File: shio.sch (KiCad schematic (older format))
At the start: 36 parts

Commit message: Few additions
- Added USB micro
- Added 2 LEDs
- Swapped NOR for NAND memory
- Added test points
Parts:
- removed U?: W25Q16JVSSIQ, SOIC127P790X216-8N, symbol W25Q16JVSSIQ:W25Q16JVSSIQ
- added AE?: Antenna_Chip, symbol Device:Antenna_Chip
- added D?: LED1, symbol Device:LED_Small_ALT
- added D?: LED2, symbol Device:LED_Small_ALT
- added J?: USB_B_Micro, symbol Connector:USB_B_Micro
- added R? (x2): 220R, symbol Device:R_Small_US
- added TP? (x15): TestPoint, symbol Connector:TestPoint
- added U?: W25N01GVZEIG_TR, SON127P800X600X80-9N, symbol W25N01GVZEIG_TR:W25N01GVZEIG_TR
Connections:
- net labels added: GPIO1, GPIO2, GPIO3, GPIO4, PDM_DATA_EXT
- net labels removed: ANT, DEBUG_UART_CTS, DEBUG_UART_RTS, DEBUG_UART_RX, DEBUG_UART_TX
- wire segments 139 -> 170
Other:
- moved on the sheet: C?, R?, S?, U?A

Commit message: swap out part for the BGA symbol
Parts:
- removed C? (x2): 12pF, symbol Device:C_Small
- removed C?: .8pF, symbol Device:C
- removed C?: 100pF, symbol Device:C
- removed C?: 1uF, symbol Device:C
- removed C?: 47nF, symbol Device:C
- removed C? (x3): 4.7uF, symbol Device:C
- removed U?: nRF52840, Package_DFN_QFN:Nordic_AQFN-73-1EP_7x7mm_P0.5mm, symbol MCU_Nordic:nRF52840
- removed Y?: 32.768KHz, symbol Device:Crystal_Small
- added C? (x3): 4.7uF, symbol Device:C
- added C?: 47nF, symbol Device:C
- added C?: 1uF, symbol Device:C
- added L?: 4.7nH, symbol Device:L
- added TP? (x2): TestPoint, symbol Connector:TestPoint
- added U? (x3): NRF52840-CKAA-R7, BGA94N35P10X10_360X354X51N, symbol NRF52840-CKAA-R7:NRF52840-CKAA-R7
- C?: value .5pF -> 1pF
- L?: value L -> 3.9nH
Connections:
- net labels added: BUTTON
- net labels removed: D_N, D_P, PDM_DATA_EXT
- wire segments 170 -> 148
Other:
- moved on the sheet: BAT?, C?, D?, J?, L?, MK?, R?, S?, TP?, U?, U?A, U?B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

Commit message: Add 0R resistors
- Add option to short VBAT to VDD_nRF and bypass switches
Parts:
- added R? (x2): NC, symbol Device:R_Small_US
- added R? (x16): 0R, symbol Device:R_Small_US
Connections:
- wire segments 148 -> 152

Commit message: Generated netlist
- Matched up some symbols with their footprints
- Need to find footprint for coin cell and micro usb
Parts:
- removed AE?: Antenna_Chip, symbol Device:Antenna_Chip
- added ANT1: 2450AT18A100E, digikey-footprints:Antenna_1.6x3.2mm_2450AT18A100E, symbol dk_RF-Antennas:2450AT18A100E
- C1, C10, C13, C3, C5: renamed from C?; footprint (none) -> Capacitor_SMD:C_0402_1005Metric
- C11, C12, C14, C15, C2, C4, C6, C7, C8, C9: renamed from C?; footprint (none) -> Capacitor_SMD:C_0201_0603Metric
- D1, D2: renamed from D?; footprint (none) -> LED_SMD:LED_0402_1005Metric
- L1, L3, L4: renamed from L?; footprint (none) -> Inductor_SMD:L_0201_0603Metric
- L2: renamed from L?; footprint (none) -> Inductor_SMD:L_0603_1608Metric
- MK1: renamed from MK?; footprint MIC_ICS-41350 -> maruchi-kicad-library:MIC_ICS-41350
- R1, R10, R11, R12, R13, R14, R15, R16, R17, R18, R19, R2, R20, R21, R3, R4, R5, R6, R7, R8, R9: renamed from R?; footprint (none) -> Resistor_SMD:R_0201_0603Metric
- TP1, TP10, TP11, TP12, TP13, TP14, TP15, TP16, TP17, TP2, TP3, TP4, TP5, TP6, TP7, TP8, TP9: renamed from TP?; footprint (none) -> TestPoint:TestPoint_Pad_D1.0mm
- U1: renamed from U?; footprint BGA94N35P10X10_360X354X51N -> maruchi-kicad-library:BGA94N35P10X10_360X354X51N
- U4: renamed from U?; footprint SON127P800X600X80-9N -> maruchi-kicad-library:SON127P800X600X80-9N
- U5: renamed from U?; footprint XDCR_BMA400 -> maruchi-kicad-library:XDCR_BMA400
- Y1: renamed from Y?; footprint (none) -> Crystal:Crystal_SMD_2016-4Pin_2.0x1.6mm
- gave numbers to parts that had none: 6
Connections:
- wire segments 152 -> 153
- no-connect marks 0 -> 31

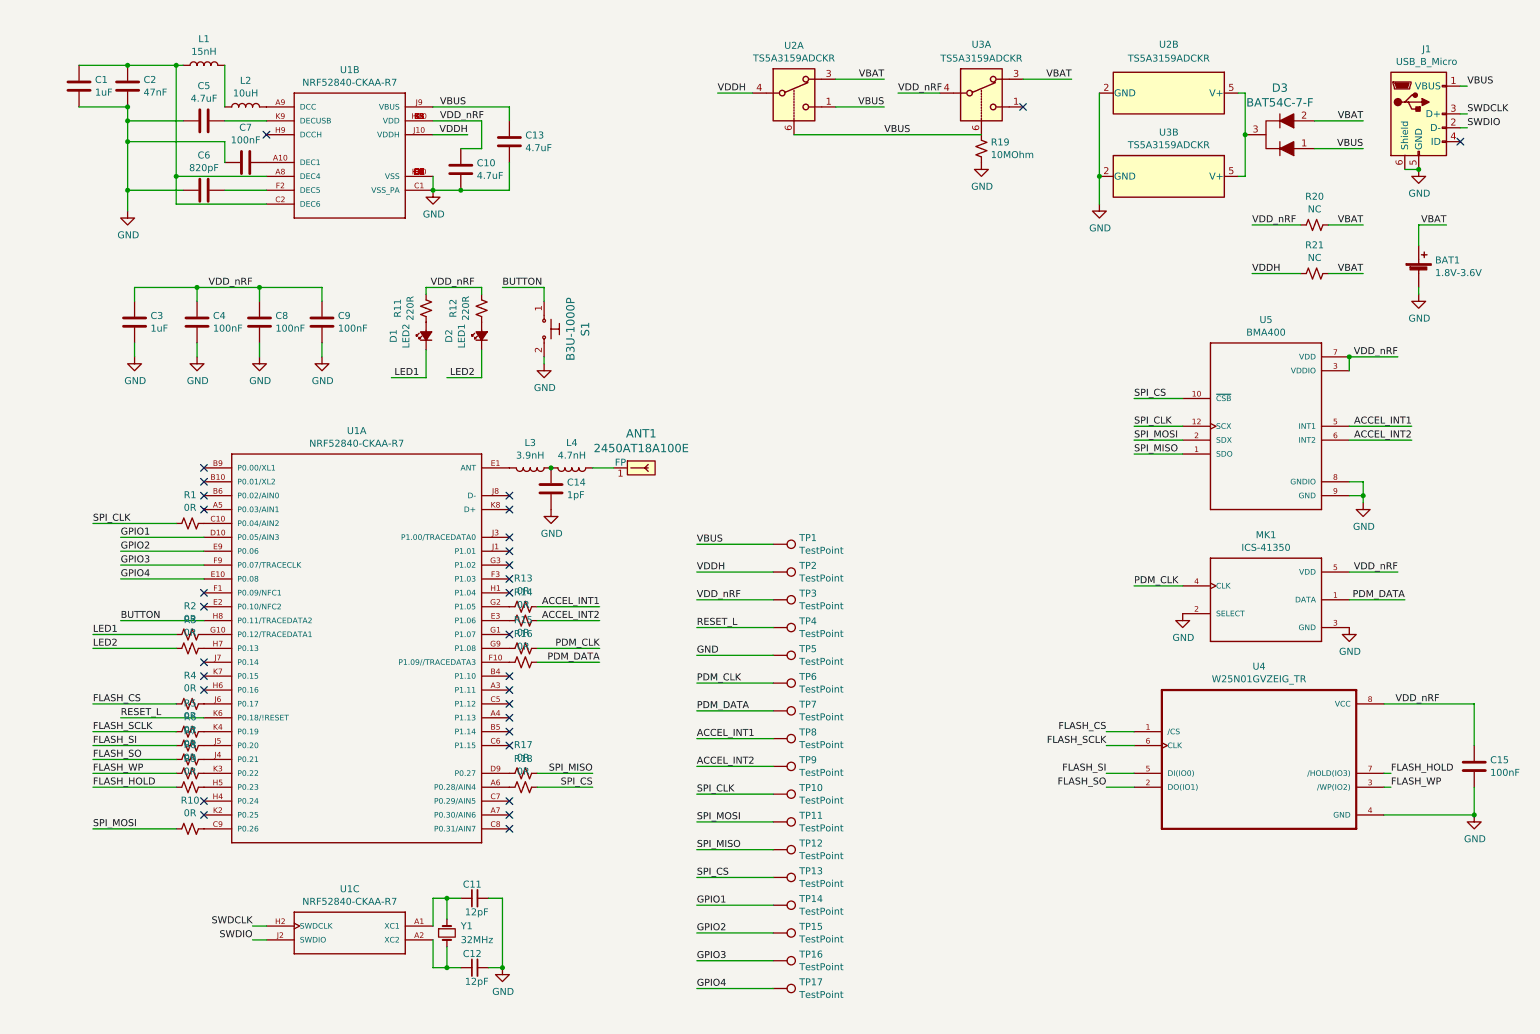
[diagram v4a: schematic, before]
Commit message: added low freq clock, style updates to schematic
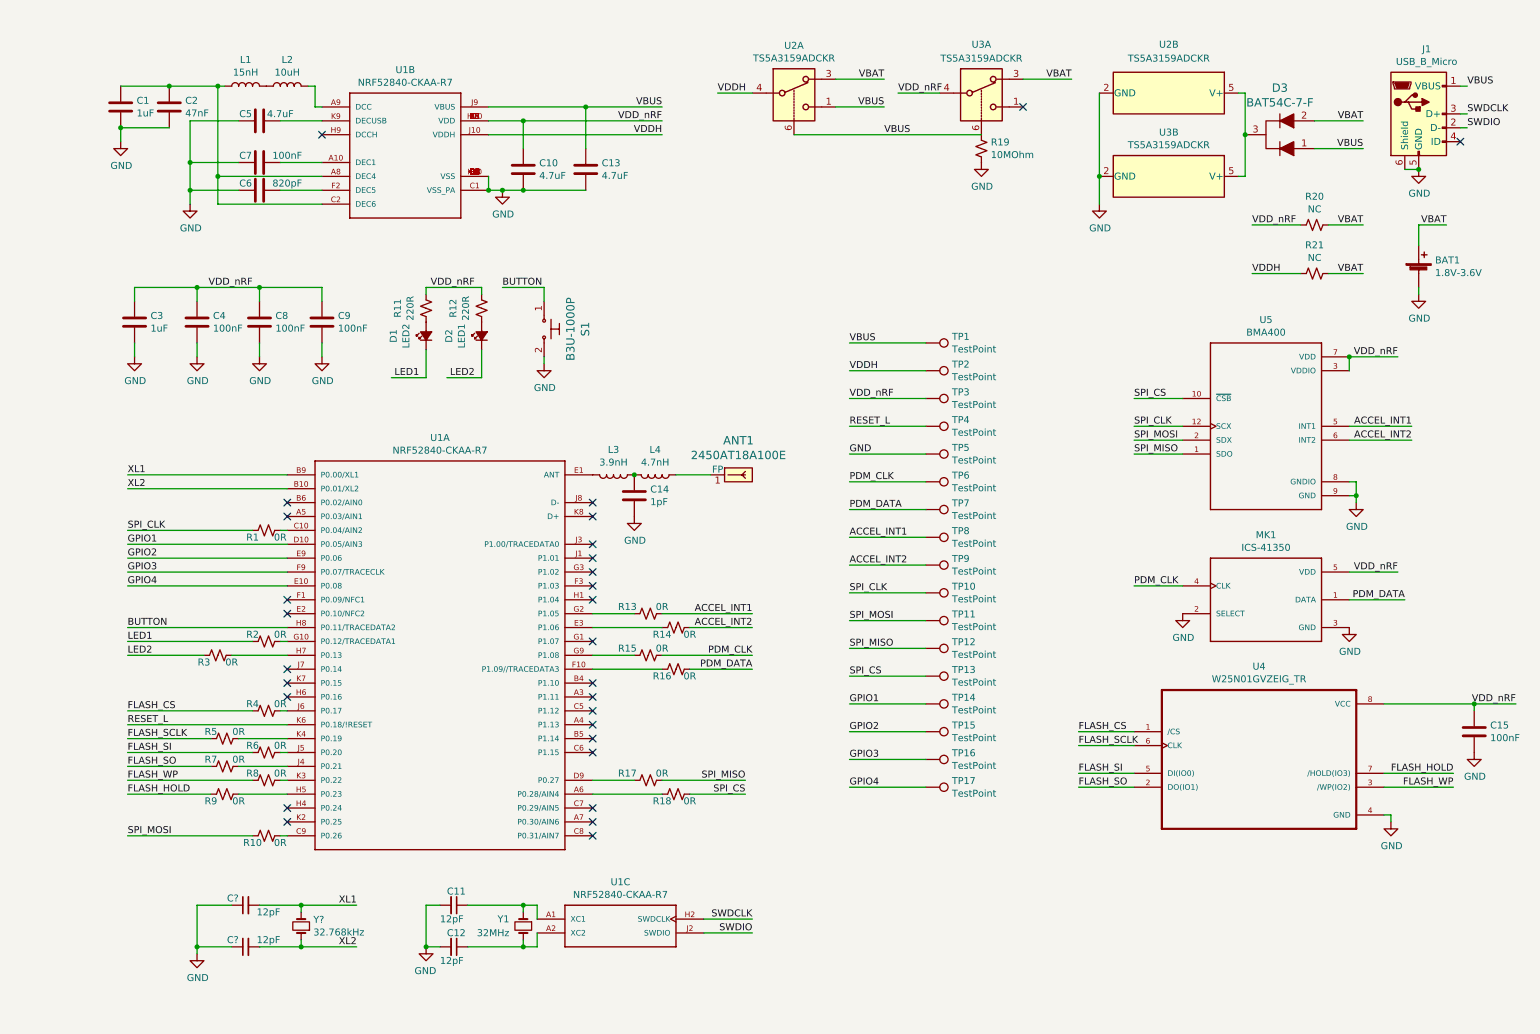
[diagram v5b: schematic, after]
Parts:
- added C? (x2): 12pF, Capacitor_SMD:C_0201_0603Metric, symbol Device:C_Small
- added Y?: 32.768kHz, symbol Device:Crystal_Small
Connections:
- net GND: now also C?.1, C?.1
- net XL2: now reaches U1.B10 (P0.01/XL2)
- net XL2: now also C?.2, Y?.1
- net XL1: now reaches U1.B9 (P0.00/XL1)
- net XL1: now also C?.2, Y?.2
- no-connect marks 31 -> 29
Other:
- moved on the sheet: ANT1, C1, C10, C11, C12, C13, C14, C15, C2, C5, C6, C7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

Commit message: Add ideal OR gates and buck converter
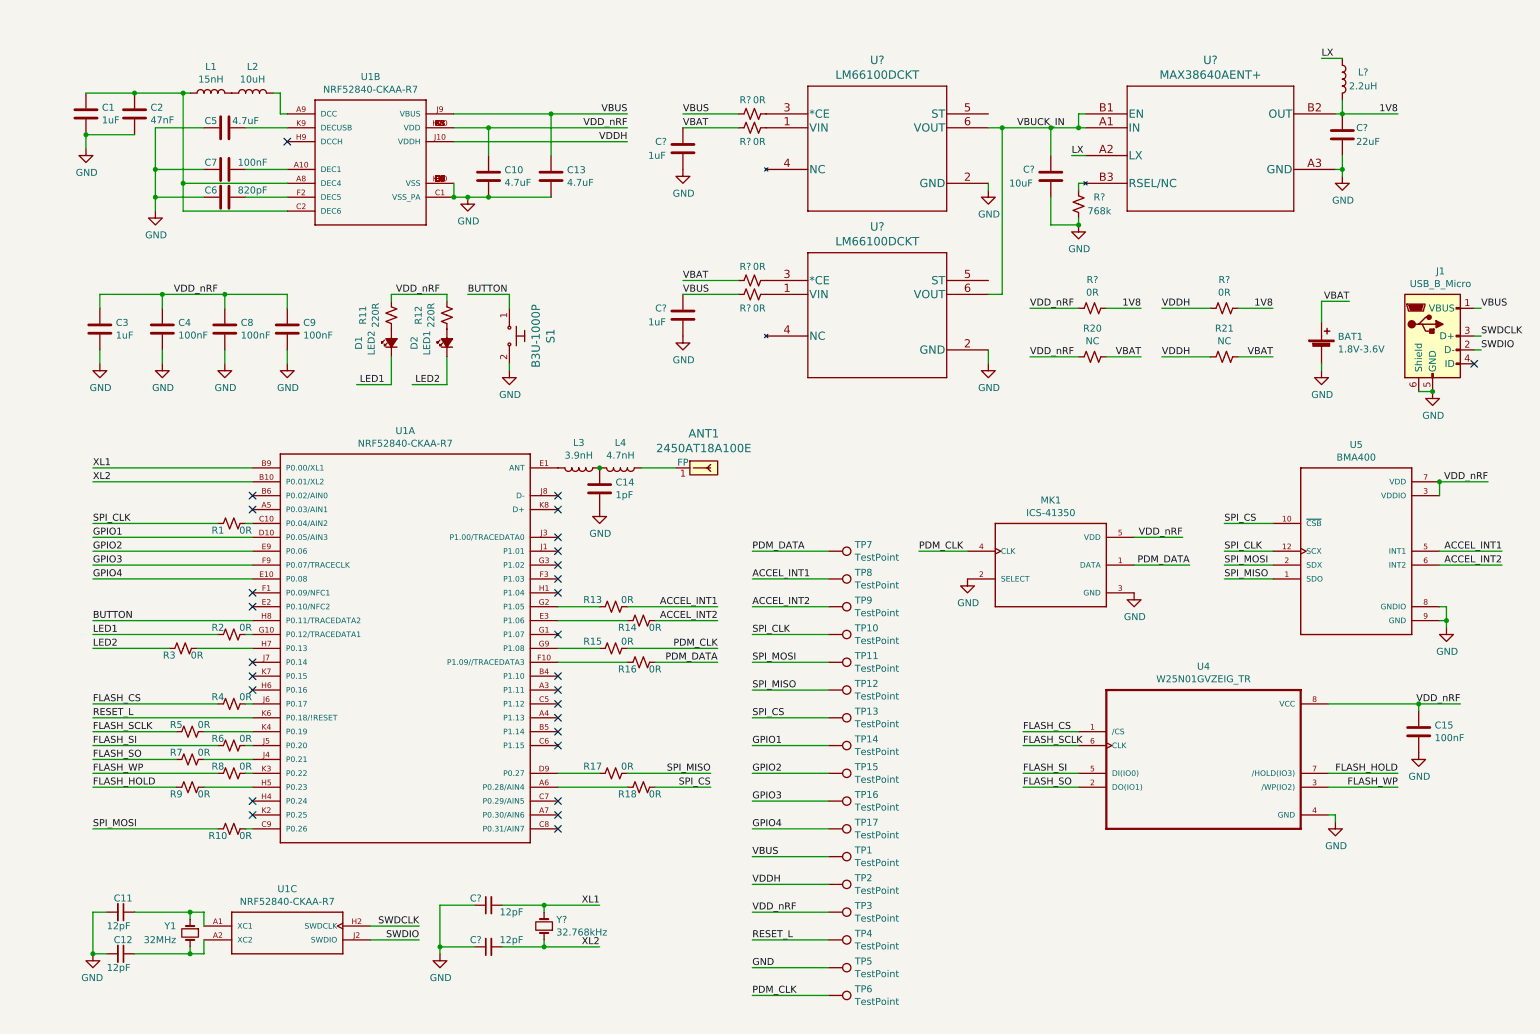
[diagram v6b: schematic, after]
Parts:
- removed D3: BAT54C-7-F, digikey-footprints:SOT-23-3, symbol dk_Diodes-Rectifiers-Arrays:BAT54C-7-F
- removed R19: 10MOhm, Resistor_SMD:R_0201_0603Metric, symbol Device:R_Small_US
- removed U2, U3: TS5A3159ADCKR, Package_TO_SOT_SMD:SOT-363_SC-70-6, symbol Analog_Switch:TS5A3159ADCKR
- added C? (x2): 1uF, Capacitor_SMD:C_0402_1005Metric, symbol Device:C
- added C?: 10uF, Capacitor_SMD:C_0402_1005Metric, symbol Device:C
- added C?: 22uF, Capacitor_SMD:C_0402_1005Metric, symbol Device:C
- added L?: 2.2uH, Inductor_SMD:L_0603_1608Metric, symbol Device:L
- added R?: 768k, Resistor_SMD:R_0201_0603Metric, symbol Device:R_Small_US
- added R? (x6): 0R, Resistor_SMD:R_0201_0603Metric, symbol Device:R_Small_US
- added U?: MAX38640AENT+, 21-100128A_6_MXM, symbol MAX38640:MAX38640AENT+
- added U? (x2): LM66100DCKT, DCK6, symbol LM66100:LM66100DCKT
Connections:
- net GND: now also C?.2, C?.2, C?.2, C?.2, R?.1, U?.2 (GND), U?.2 (GND), U?.A3 (GND)
- net VBAT: now also C?.1, R?.2, R?.2
- net VBUS: now also C?.1, R?.2, R?.2
- net VDDH: now also R?.2
- net VDD_nRF: now also R?.2
- new net: R?.2, U?.B3 (RSEL/NC)
- new net: R?.1, U?.1 (VIN) (x2)
- new net: R?.1, U?.3 (*CE) (x2)
- new net 1V8: C?.1, L?.2, R?.1, R?.1, U?.B2 (OUT)
- new net LX: L?.1, U?.A2 (LX)
- new net VBUCK_IN: C?.1, U?.6 (VOUT), U?.6 (VOUT), U?.A1 (IN), U?.B1 (EN)
- no-connect marks 29 -> 28
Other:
- moved on the sheet: ANT1, BAT1, C1, C10, C11, C12, C13, C14, C15, C2, C3, C4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

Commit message: Add footprints
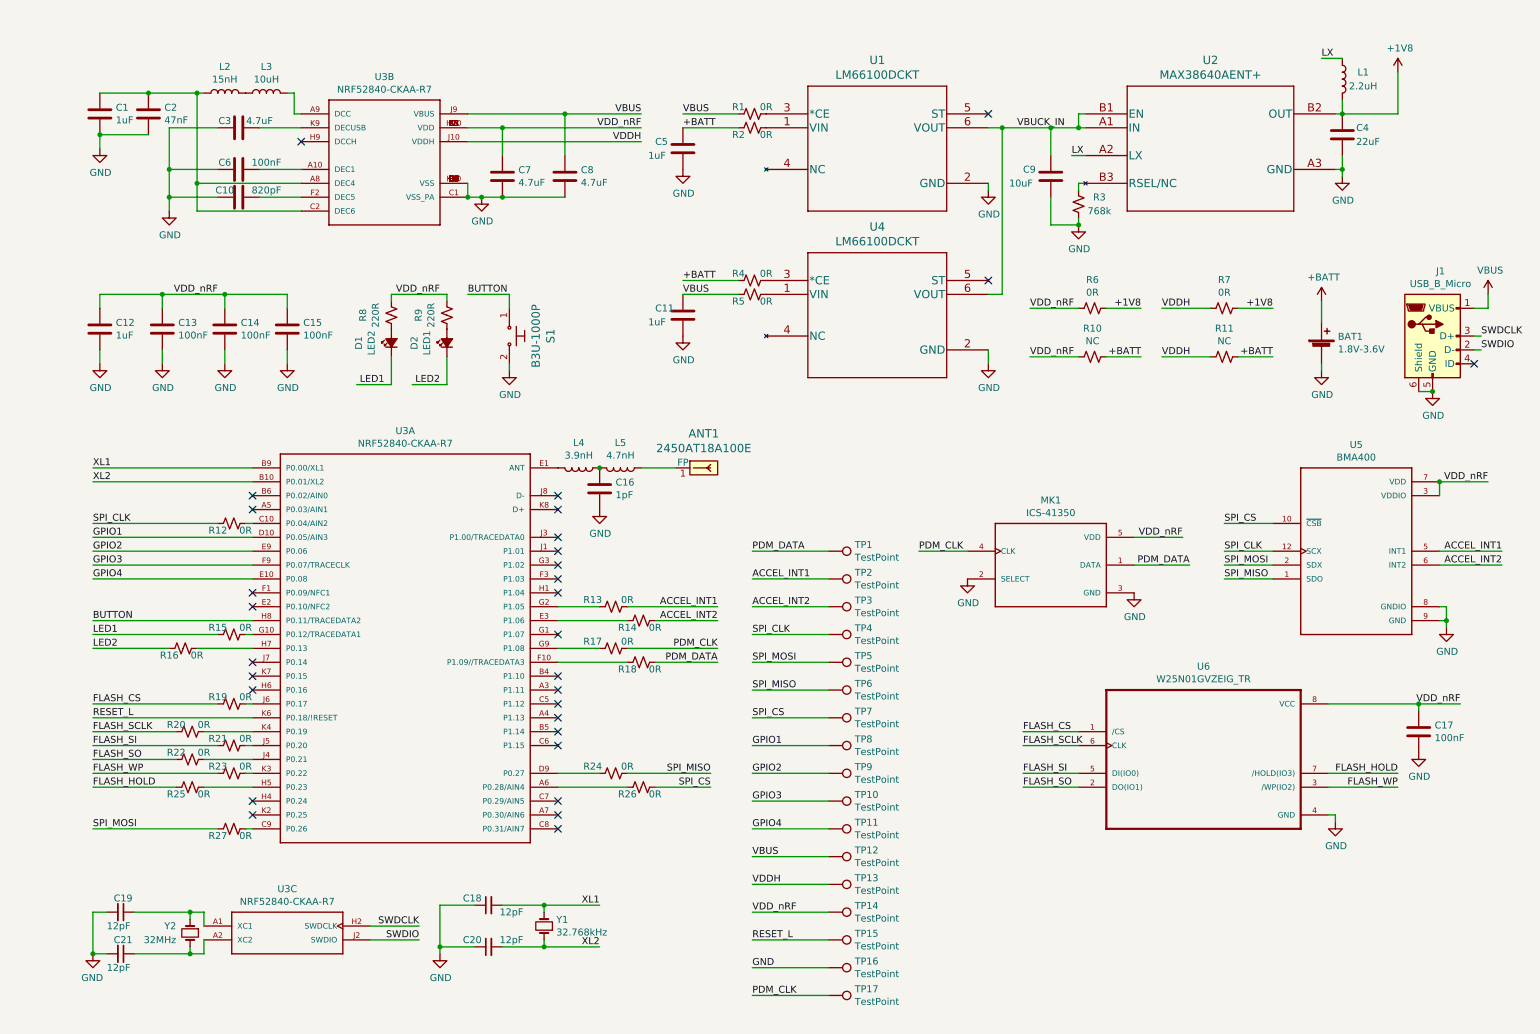
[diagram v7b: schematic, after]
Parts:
- gave numbers to parts that had none: 18
- renumbered C6 to C10, C3 to C12, C4 to C13, C8 to C14, C9 to C15, C14 to C16, C15 to C17, C11 to C19, C12 to C21, C5 to C3, C7 to C6, C10 to C7, C13 to C8, L1 to L2, L2 to L3, L3 to L4, L4 to L5, R20 to R10, R21 to R11, R1 to R12, R2 to R15, R3 to R16, R15 to R17, R16 to R18, R4 to R19, R5 to R20, R6 to R21, R7 to R22, R8 to R23, R17 to R24, R9 to R25, R18 to R26, R10 to R27, R11 to R8, R12 to R9, TP7 to TP1, TP16 to TP10, TP17 to TP11, TP1 to TP12, TP2 to TP13, TP3 to TP14, TP4 to TP15, TP5 to TP16, TP6 to TP17, TP8 to TP2, TP9 to TP3, TP10 to TP4, TP11 to TP5, TP12 to TP6, TP13 to TP7, TP14 to TP8, TP15 to TP9, U1 to U3, U4 to U6, Y1 to Y2
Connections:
- net 1V8 renamed +1V8
- net VBAT renamed +BATT
- no-connect marks 28 -> 30
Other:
- moved on the sheet: C1, C10, C2, C3, C6, C7, C8, L2, L3, U3B
